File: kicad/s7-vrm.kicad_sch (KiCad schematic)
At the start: 34 parts, among them J1 Conn_02x15_Row_Letter_First, J2 Conn_02x02_Odd_Even, Q1 Q_NPN_BEC_BRT, Q2 Q_NMOS_GDS, Q3 Q_NMOS_GDS, Q4 Q_PNP_BEC_BRT, SW1 SW_DIP_x05, U1 ISL6545

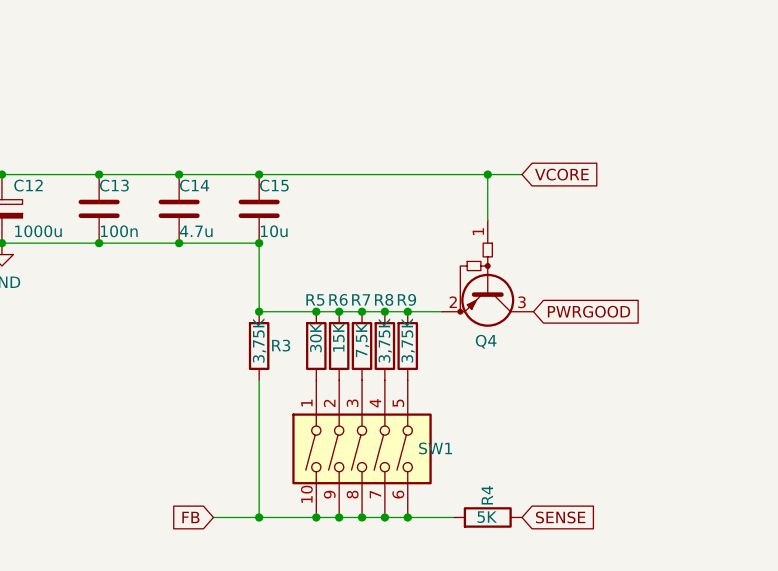
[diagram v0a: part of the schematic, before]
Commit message: Drop sense pin usage.
Some mainboards don't implement sense pin properly and have other
signals connected to that pin. This can lead to invalid output voltage
reading. In the worst case sense could be bound to ground, which would
report 0V to the controller all the time, which would try to ramp up
the voltage to the maximum of about 4.4V. This could potentially kill
the CPU, especially low voltage K6-II or similar.

Due to this issue, the feedback voltage is now read directly at the
vcore output. This could potentially lead to slightly lower output
voltage at the CPU, since we would not read the sense from there, but
it is much safer and would work on more mainboards.
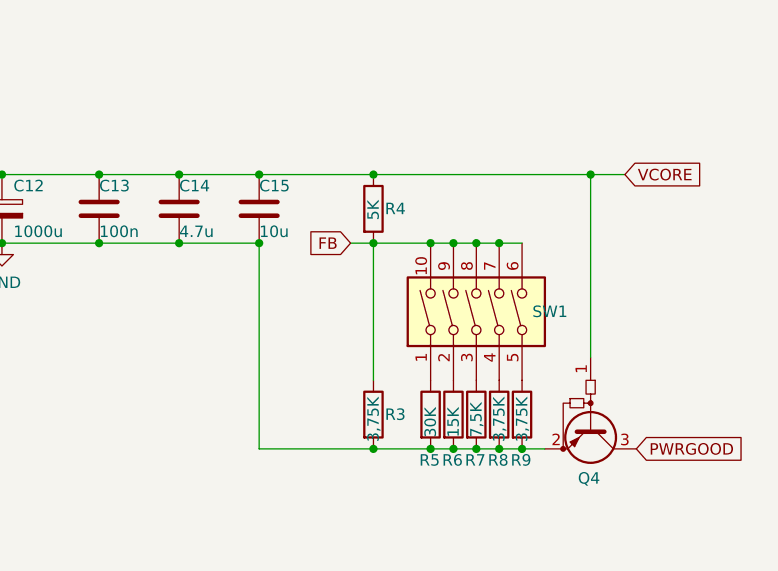
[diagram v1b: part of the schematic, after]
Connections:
- net SENSE: no longer R4.1
- net VCORE: now also R4.1
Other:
- moved on the sheet: Q4, R3, R4, R5, R6, R7, R8, R9, SW1
